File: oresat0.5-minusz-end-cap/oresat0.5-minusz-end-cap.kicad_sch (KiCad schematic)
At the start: 35 parts, among them J2 U.FL-R-SMA, U2 MMC5883MA, U3 MMC5883MA

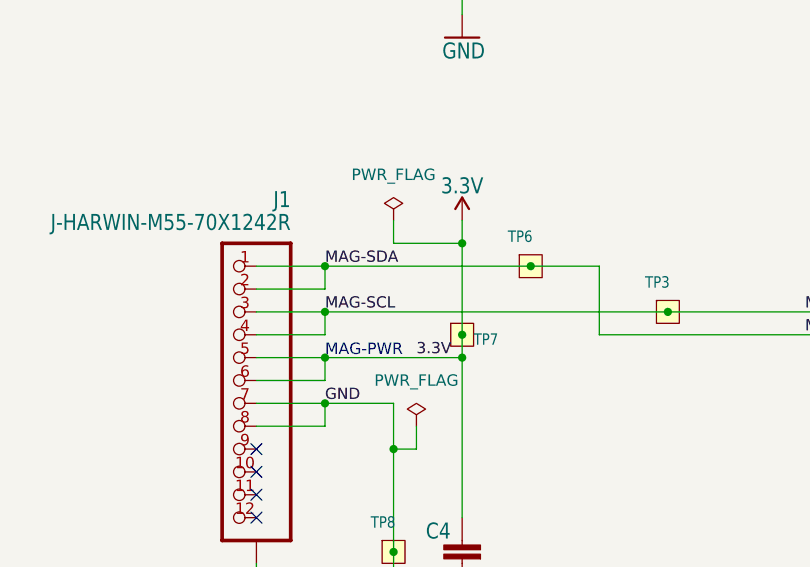
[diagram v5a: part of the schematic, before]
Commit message: OreSat0.5 -Z end cap. Updated to latest KiCAD, fixed lack of holes for lens holder, and removed solder mask from around screw heads.
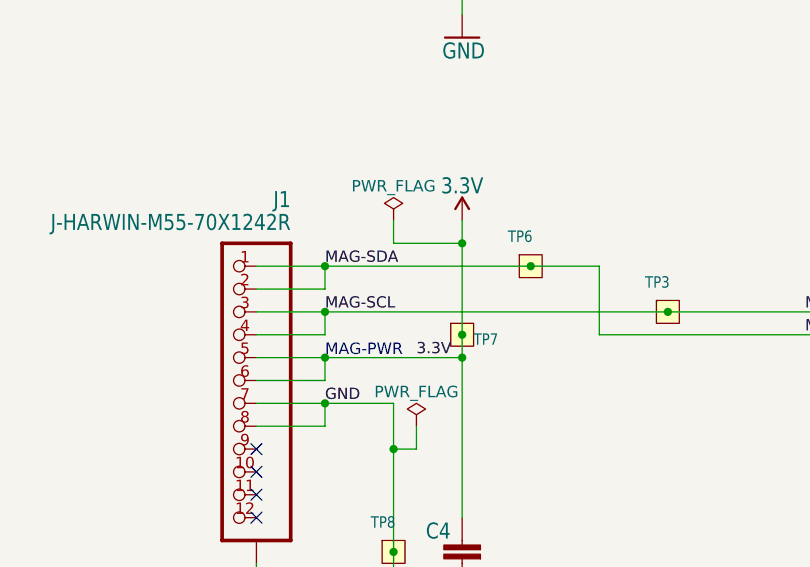
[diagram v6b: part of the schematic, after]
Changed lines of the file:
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@@
       (effects (font (size 1.27 1.27)) hide)
     )
-    (property "Value" "PWR_FLAG" (at 119.38 124.46 0)
+    (property "Value" "PWR_FLAG" (at 119.38 125.73 0)
       (effects (font (size 1.27 1.27)))
     )
@@
       (effects (font (size 1.27 1.27)) hide)
     )
-    (property "Value" "PWR_FLAG" (at 116.84 101.6 0)
+    (property "Value" "PWR_FLAG" (at 116.84 102.87 0)
       (effects (font (size 1.27 1.27)))
     )

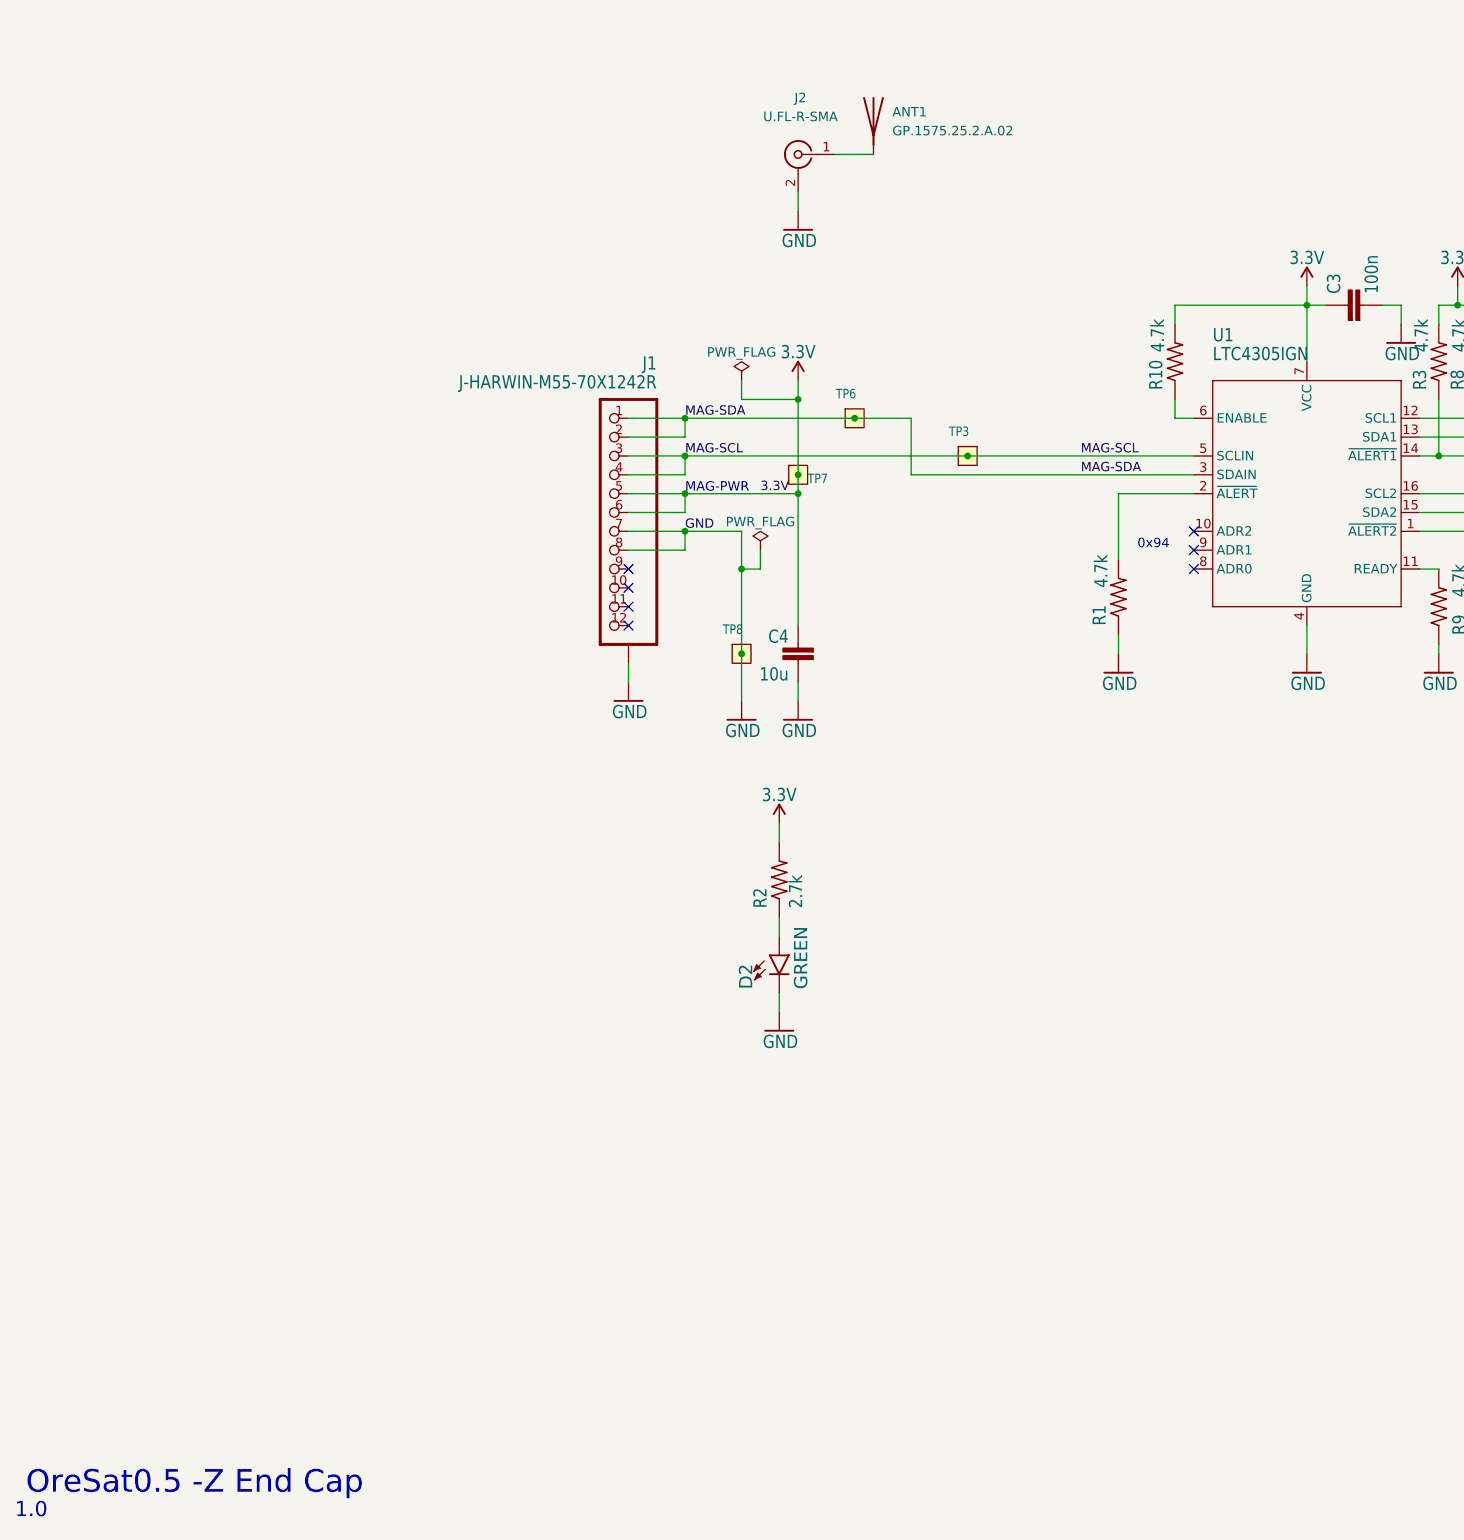
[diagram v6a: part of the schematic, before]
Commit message: Small changes to schematic, mostly comments.
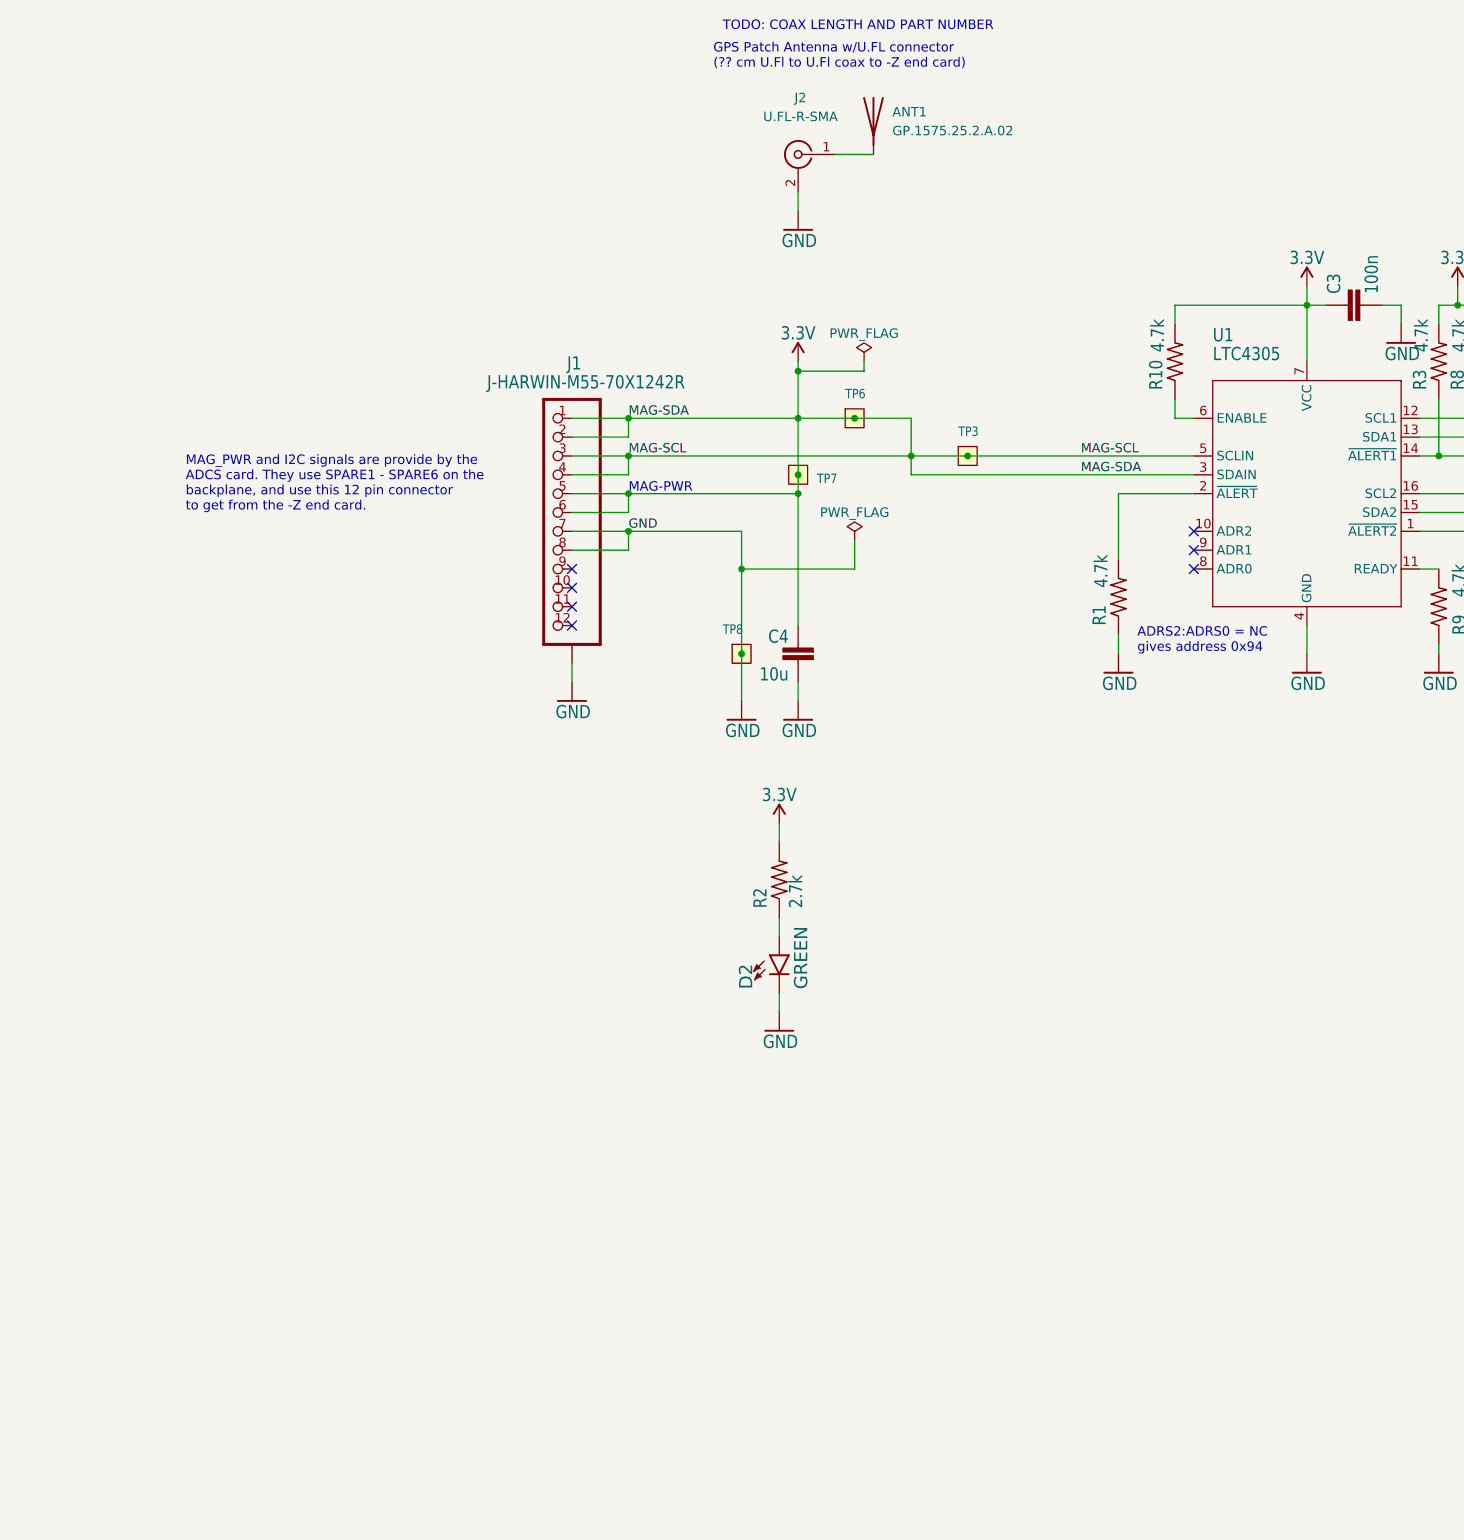
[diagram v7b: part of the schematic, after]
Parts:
- U1: value (none) -> LTC4305; footprint oresat0.5-minusz-end-cap:16-SSOP -> oresat0-plusz-end-cap:16-SSOP; symbol oresat0.5-minusz-end-cap-eagle-import:LTC4305 -> oresat-ics:LTC4305
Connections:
- net MAG-SCL is gone; now on net 3.3V: J1.3, J1.4, TP3.1, U1.5 (SCLIN)
- net MAG-SDA is gone; now on net 3.3V: J1.1, J1.2, TP6.1, U1.3 (SDAIN)
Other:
- note added: "ADRS2:ADRS0 = NC gives address 0x94"
- note added: "GPS Patch Antenna w/U.FL connector (?? cm U.Fl to U.Fl coax to -Z end card)"
- note added: "MAG_PWR and I2C signals are provide by the ADCS card. They use SPARE1 - SPARE6 on the backplane, and use this 12 pin connector to get from the -Z end card."
- note added: "TODO: COAX LENGTH AND PART NUMBER"
- note removed: "0x94"
- note removed: "1.0"
- note removed: "OreSat0.5 -Z End Cap"
- title: (none) -> OreSat0.5 -Z End Cap
- moved on the sheet: J1

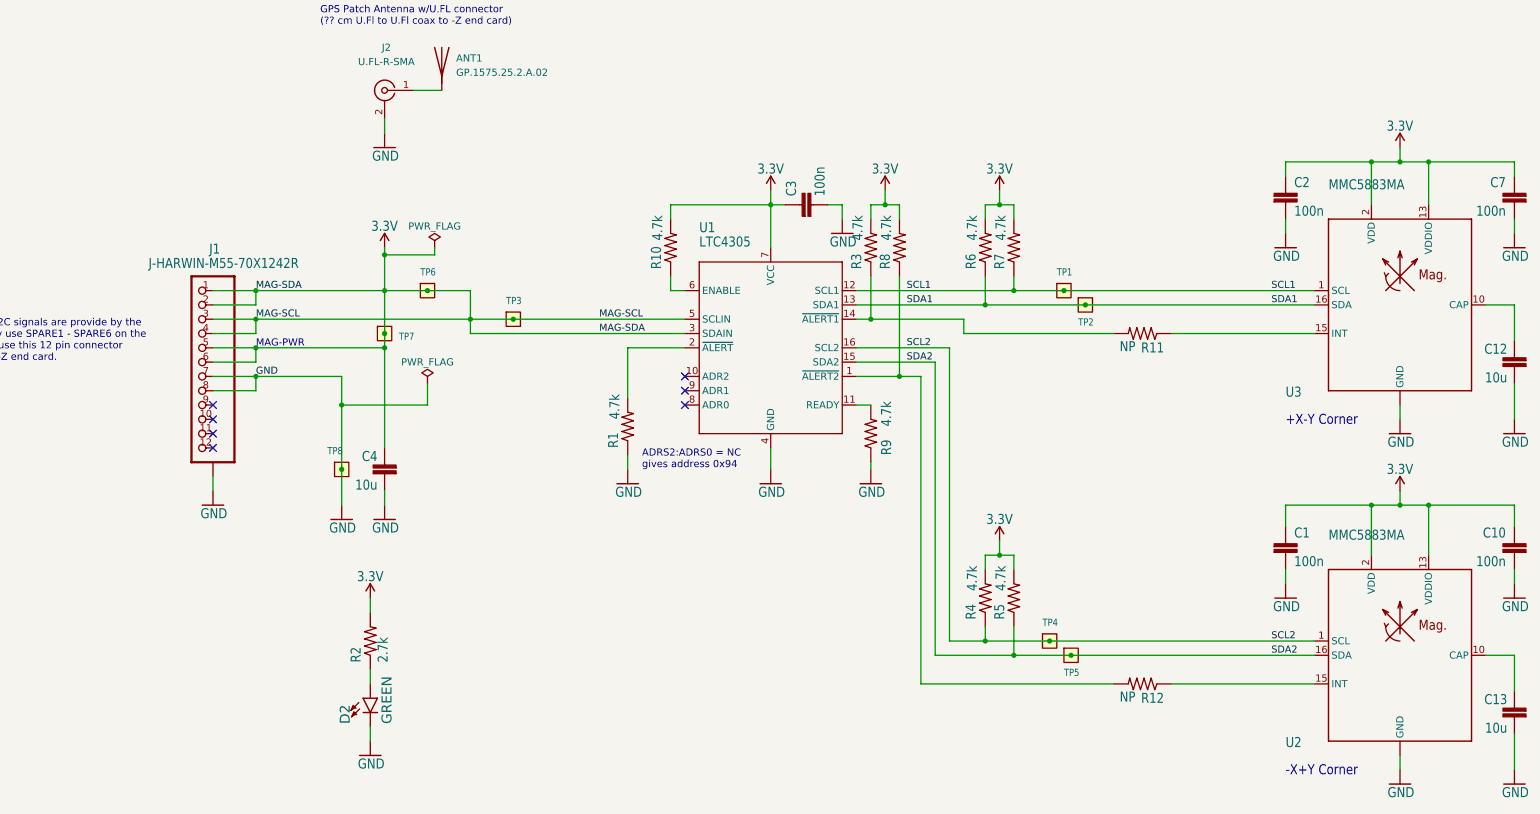
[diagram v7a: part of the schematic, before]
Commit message: updated mmc5883 magnetometer to mmc5983 for both OreSat 0.5 +Z and -Z endcaps
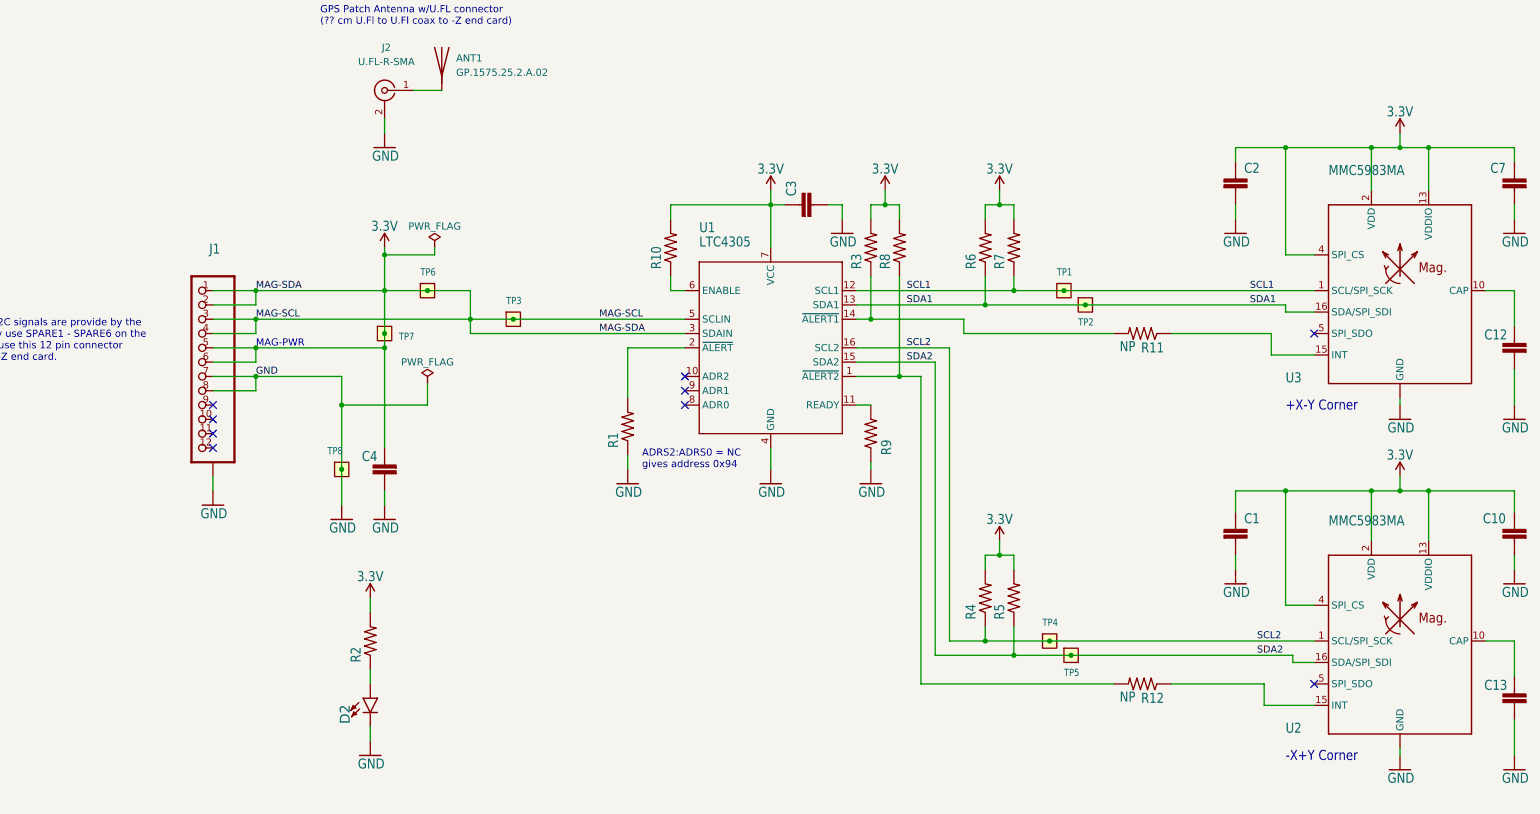
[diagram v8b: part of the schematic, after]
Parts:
- U2, U3: value MMC5883MA -> MMC5983MA; footprint oresat0-plusz-end-cap:LGA-16(3X3) -> oresat-ics:LGA-16(3X3); symbol oresat0.5-minusz-end-cap-eagle-import:MMC5883MA -> oresat-ics:MMC5983MA
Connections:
- net 3.3V: now also U2.4 (SPI_CS), U3.4 (SPI_CS)
- no-connect marks 7 -> 9
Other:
- moved on the sheet: C1, C10, C12, C13, C2, C7
